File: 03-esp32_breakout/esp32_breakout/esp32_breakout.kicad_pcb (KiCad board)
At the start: 4 copper layers, 35 x 22.8 mm, 44 parts, among them J1 USB4110-GF-A, J2 Conn_01x06, SW1 SW_Push, SW2 SW_Push, SW3 SW_Push, U1 ESP32-S3, U3 AP2112H, Y1 ECS-400-10-37B2-CKY-TR, Y2 ECS-.327-12.5-34B-TR

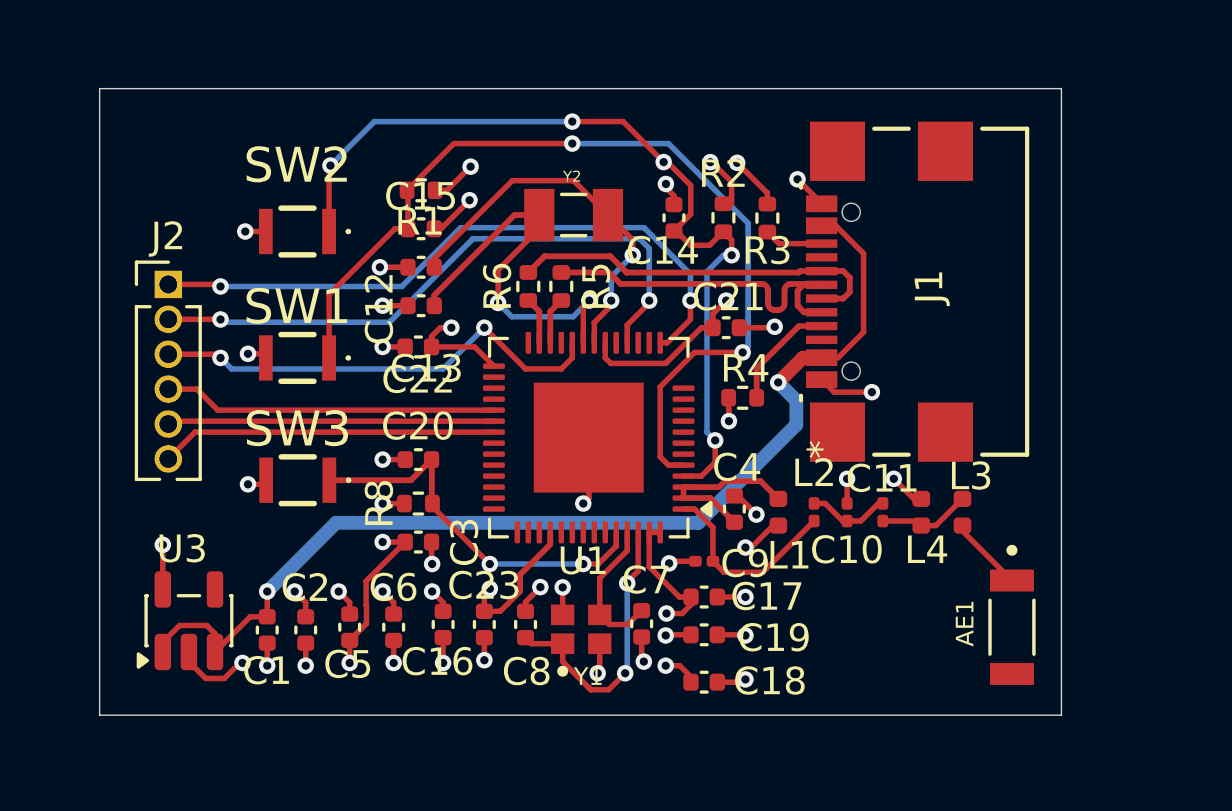
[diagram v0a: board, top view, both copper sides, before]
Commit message: layout improvement
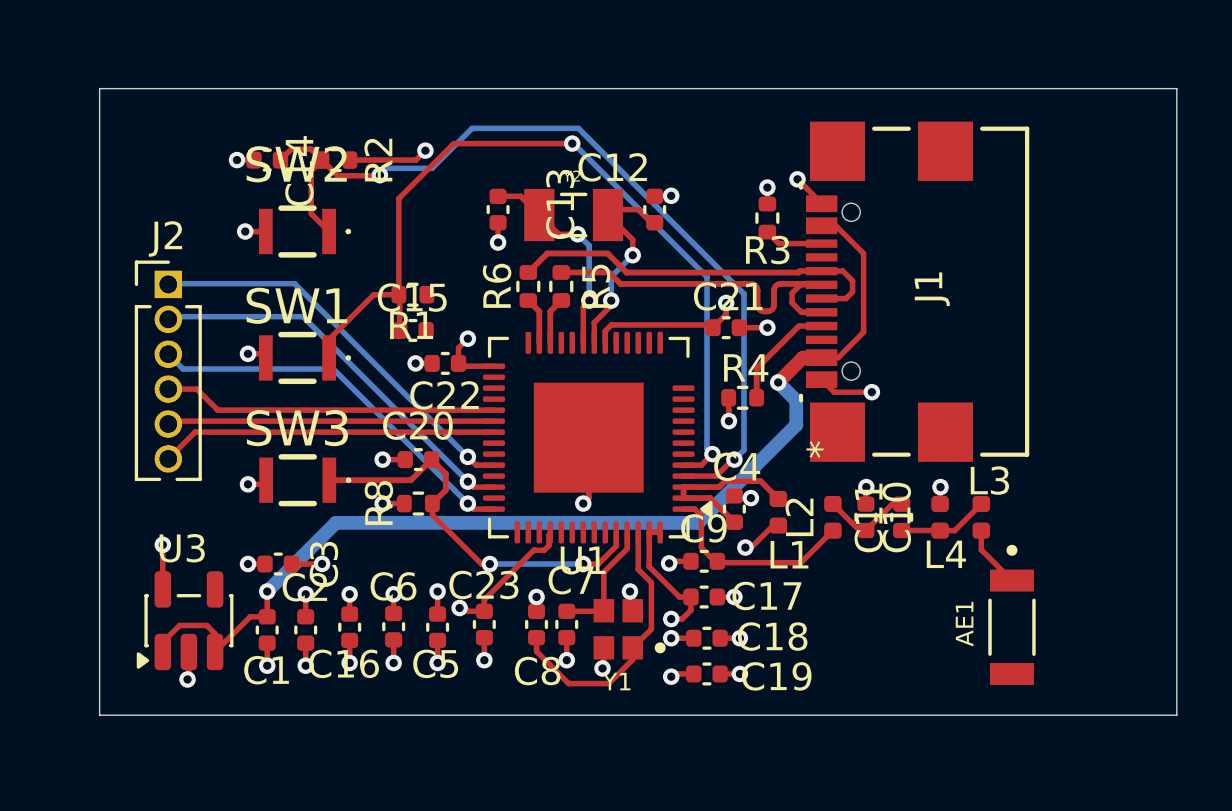
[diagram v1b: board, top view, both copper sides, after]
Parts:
- C10, C11, C9: footprint Capacitor_SMD:C_0201_0603Metric -> Capacitor_SMD:C_0402_1005Metric
- L2: footprint Inductor_SMD:L_0201_0603Metric -> Inductor_SMD:L_0402_1005Metric
- moved C14 14.9 mm to (153.5, 50.6), turned to 180 degrees
- moved R2 14.3 mm to (156.0, 50.6), turned to 0 degrees
- moved C12 8.76 mm to (167.6, 52.4), turned to -90 degrees
- moved C3 5.16 mm to (153.9, 65.3)
- moved C13 4.48 mm to (161.9, 52.4), turned to 90 degrees
- moved R1 3.81 mm to (158.8, 55.5)
- moved C15 3.71 mm to (158.8, 56.8)
- moved C16 3.40 mm to (156.5, 67.6)
- moved C5 3.20 mm to (159.7, 67.6)
- moved C7 2.73 mm to (164.4, 67.5)
- moved C18 1.60 mm to (169.5, 68.0)
- moved C19 1.43 mm to (169.5, 69.3)
- moved Y1 1.35 mm to (166.3, 67.7), turned to 90 degrees
- moved C22 1.15 mm to (160.0, 58.0)
- moved C10 0.71 mm to (175.3, 63.6)
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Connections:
- U1 pad 15: CS_FLASH -> unconnected-(U1-GPIO10-Pad15)
- U1 pad 18: CS_DAC -> unconnected-(U1-GPIO13-Pad18)
- U1 pad 23: CS_ADC -> unconnected-(U1-GPIO17-Pad23)
- U1 pad 38: unconnected-(U1-GPIO33-Pad38) -> CS_FLASH
- U1 pad 40: unconnected-(U1-GPIO35-Pad40) -> CS_DAC
- U1 pad 42: unconnected-(U1-GPIO37-Pad42) -> CS_ADC
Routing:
- net GND: track 42.8 -> 28.2 mm, vias 34 -> 33
- net CS_FLASH: track 23.7 -> 14.6 mm, vias 2 -> 1
- net CS_DAC: track 22.8 -> 14.5 mm, vias 2 -> 1
- net Net-(U1-XTAL_32K_N): track 15.2 -> 8.35 mm
- net Net-(U1-XTAL_32K_P): track 13.9 -> 7.58 mm
- net  VDD3P3_RTC: track 34.6 -> 31.0 mm, vias 16 -> 15
- net GPIO0: track 33.7 -> 30.5 mm
- net CS_ADC: track 16.9 -> 14.2 mm, vias 2 -> 1
- net Net-(U1-XTAL_N): track 5.29 -> 4.56 mm
- net Net-(C10-Pad2): track 3.03 -> 3.62 mm
- net GPIO46: track 14.1 -> 14.7 mm
- net Net-(U1-XTAL_P): track 10.4 -> 9.95 mm, vias 2 -> 0
- net Chip_PU: track 31.9 -> 32.2 mm, vias 5 -> 2
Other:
- board size 35 x 22.8 mm -> 39.2 x 22.8 mm

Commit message: ground zone
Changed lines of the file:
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@@
+	)
+	(segment
+		(start 168.18 51.92)
+		(end 167.6 51.92)
+		(width 0.2)
+		(layer "F.Cu")
+		(net 1)
 	)
 	(segment
@@
 	)
 	(segment
-		(start 168.18 51.92)
-		(end 168.2 51.9)
-		(width 0.2)
-		(layer "F.Cu")
-		(net 1)
-	)
-	(segment
 		(start 177.985 63.115)
 		(end 177.985 62.515)
@@
 	)
 	(segment
+		(start 168.3 51.8)
+		(end 168.18 51.92)
+		(width 0.2)
+		(layer "F.Cu")
+		(net 1)
+	)
+	(segment
 		(start 177.985 62.515)
 		(end 178 62.5)
@@
 	)
 	(segment
-		(start 167.6 51.92)
-		(end 168.18 51.92)
-		(width 0.2)
-		(layer "F.Cu")
-		(net 1)
-	)
-	(segment
 		(start 170.29 59.69)
 		(end 170.29 59.25)
@@
 	)
 	(via
-		(at 168.2 51.9)
+		(at 168.3 51.8)
 		(size 0.6)
 		(drill 0.3)
@@
 		(polygon
 			(pts
-				(xy 156.6 22.6) (xy 157 36) (xy 178.8 35.9) (xy 177.1 21.7)
-			)
-		)
-	)
-	(zone
-		(net 0)
-		(net_name "")
-		(layer "In1.Cu")
-		(hatch edge 0.5)
-		(connect_pads
-			(clearance 0)
-		)
-		(min_thickness 0.25)
-		(filled_areas_thickness no)
-		(keepout
-			(tracks allowed)
-			(vias allowed)
-			(pads allowed)
-			(copperpour not_allowed)
-			(footprints allowed)
-		)
-		(placement
-			(enabled no)
-			(sheetname "/")
-		)
-		(fill
-			(thermal_gap 0.5)
-			(thermal_bridge_width 0.5)
-		)
-		(polygon
-			(pts
-				(xy 160.9 50.8) (xy 168.9 50.8) (xy 168.9 57.9) (xy 160.9 57.8)
+				(xy 161.3 51.3) (xy 168.6 51.3) (xy 168.6 57.6) (xy 161.3 57.5)
 			)
 		)
@@
 		(polygon
 			(pts
-				(xy 140.75 44) (xy 192 43.5) (xy 192 78) (xy 139.25 77)
+				(xy 192 78) (xy 139.25 77) (xy 140.75 44) (xy 192 43.5)
 			)
 		)
+		(polygon
+			(pts
+				(xy 162.5 63.6) (xy 162.5 70) (xy 167.5 69.9) (xy 167.5 63.5)
+			)
+		)
+		(polygon
+			(pts
+				(xy 160.9 57.9) (xy 168.9 57.9) (xy 168.9 50.7) (xy 160.9 50.7)
+			)
+		)
+	)
+	(zone
+		(net 1)
+		(net_name "GND")
+		(layer "In1.Cu")
+		(hatch edge 0.5)
+		(priority 3)
+		(connect_pads yes
+			(clearance 0)
+		)
+		(min_thickness 0.25)
+		(filled_areas_thickness no)
+		(fill yes
+			(thermal_gap 0.5)
+			(thermal_bridge_width 0.5)
+		)
+		(polygon
+			(pts
+				(xy 167.3 63.8) (xy 167.3 69.5) (xy 162.8 69.5) (xy 162.8 63.8)
+			)
+		)

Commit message: updated atenna layout
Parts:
- moved C3 3.88 mm to (150.1, 64.5)
- moved C8 3.53 mm to (166.8, 67.7)
- moved C9 3.45 mm to (172.3, 63.4), turned to -90 degrees
- moved C2 3.37 mm to (153.2, 64.8), turned to 180 degrees
- moved L4 2.40 mm to (180.4, 63.6)
- moved L3 2.27 mm to (181.6, 64.5)
- moved C11 2.21 mm to (178.8, 63.9), turned to 180 degrees
- moved Y1 1.24 mm to (165.0, 67.7)
- moved C7 1.19 mm to (163.2, 67.6)
- moved C10 1.01 mm to (175.6, 64.5), turned to 90 degrees
- moved L1 0.86 mm to (171.3, 63.1)
- moved AE1 0.59 mm to (180.7, 68.2)
- moved C4 0.54 mm to (170.0, 63.1), turned to 90 degrees
- moved L2 0.38 mm to (173.9, 63.9), turned to 0 degrees
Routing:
- net  VDD3P3_RTC: track 31.0 -> 48.5 mm, vias 15 -> 11
- net Net-(U1-XTAL_P): track 9.95 -> 6.12 mm
- net Net-(C4-Pad2): track 6.42 -> 3.10 mm
- net Net-(C11-Pad1): track 3.54 -> 2.37 mm
- net Net-(C10-Pad2): track 3.62 -> 4.62 mm, vias 0 -> 1
- net Net-(U1-LNA_IN): track 7.41 -> 6.83 mm
- net Net-(U1-XTAL_N): track 4.56 -> 5.07 mm

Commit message: l
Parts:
- moved R6 8.76 mm to (171.8, 55.2), turned to 180 degrees
- moved R4 8.67 mm to (171.9, 50.6)
- moved R5 7.70 mm to (171.8, 56.5), turned to 180 degrees
- moved C21 2.72 mm to (167.6, 55.9)
- moved C4 1.99 mm to (170.7, 61.3), turned to -90 degrees
- moved L1 1.94 mm to (171.9, 61.3)
- moved AE1 1.56 mm to (181.0, 69.7)
- moved J1 1.12 mm to (178.2, 55.4)
- moved R3 1.12 mm to (172.8, 52.8)
- moved C11 0.97 mm to (178.5, 64.8)
- moved L3 0.75 mm to (181.6, 65.3)
- moved L4 0.74 mm to (180.2, 64.3)
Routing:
- net USB_D-: track 14.1 -> 3.24 mm
- net USB_D+: track 14.2 -> 3.91 mm
- net Net-(J1-CC1): track 4.07 -> 12.1 mm, vias 0 -> 2
- net /ESP_USB_D+: track 1.71 -> 8.82 mm
- net Chip_PU: track 32.2 -> 25.4 mm
- net /ESP_USB_D-: track 1.71 -> 7.31 mm
- net Net-(U1-LNA_IN): track 6.83 -> 5.01 mm
- net GND: track 28.4 -> 27.0 mm, vias 33 -> 65
- net Net-(C4-Pad2): track 3.10 -> 4.26 mm
- net Net-(C10-Pad2): track 4.62 -> 3.86 mm, vias 1 -> 0
- net  VDD3P3_RTC: track 48.5 -> 47.8 mm
- net Net-(AE1-FEED): track 1.83 -> 2.46 mm
- added copper zone on F.Cu, net GND
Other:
- board size 39.2 x 22.8 mm -> 35 x 24 mm

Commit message: finish layout
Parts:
- moved R5 2.33 mm to (170.4, 58.4)
- moved R6 2.19 mm to (170.4, 57.0)
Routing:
- net USB_D-: track 3.24 -> 8.08 mm
- net USB_D+: track 3.91 -> 7.59 mm
- net /ESP_USB_D-: track 7.31 -> 8.18 mm

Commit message: fixed a few things
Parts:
- added J4: GRPB021VWVN-RC, Connector_PinHeader_1.27mm:PinHeader_1x02_P1.27mm_Vertical, F.Cu at (160.7, 70.7)
- AE1: value Antenna_Chip -> XDCR_2459AT18B100E
- C7, C8: value 14µF -> 14pF
- J2: value Conn_01x06 -> GRPB061VWVN-RC
- U3: value AP2112H -> AP2112K
- moved C7 0.29 mm to (163.5, 67.6)
- moved C8 0.29 mm to (167.1, 67.7)
- moved Y1 0.29 mm to (165.3, 67.7)
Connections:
- U1 pad 49: unconnected-(U1-U0TXD-Pad49) -> TX
- U1 pad 50: unconnected-(U1-U0RXD-Pad50) -> RX
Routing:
- net TX: track 0.00 -> 11.4 mm
- net RX: track 0.00 -> 8.78 mm

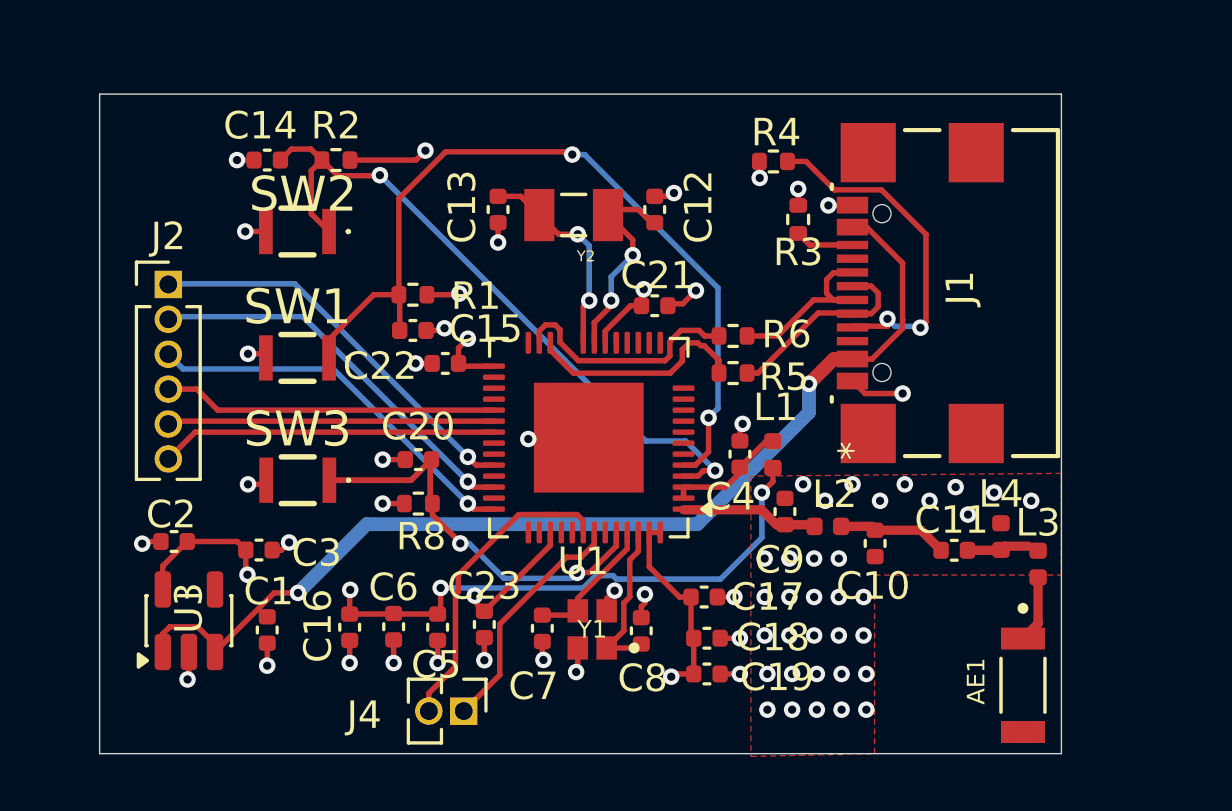
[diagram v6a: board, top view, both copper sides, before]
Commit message: added more breakout pins + added back silkscreen
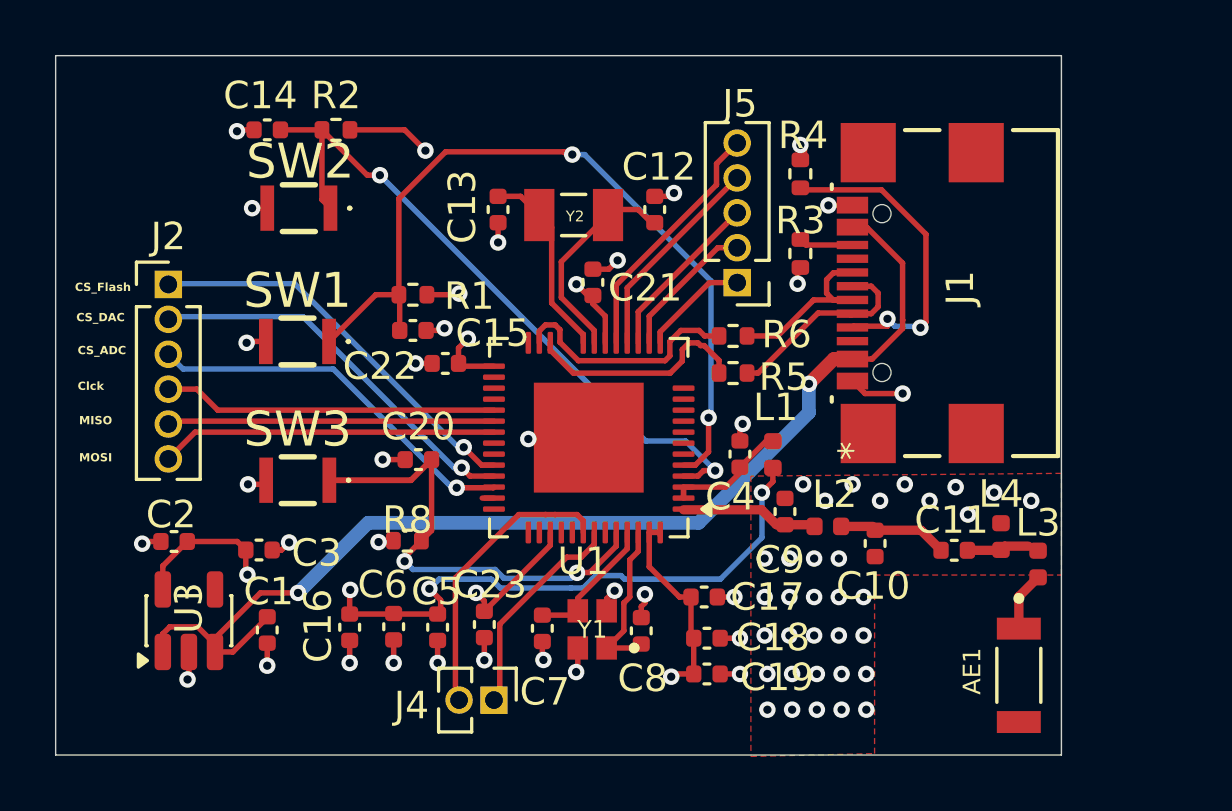
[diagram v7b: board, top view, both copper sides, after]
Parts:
- added G***: BJR_LOGO, wsg_fp:BJR_LOGO, B.Cu at (161.7, 51.0)
- added J5: GRPB051VWVN-RC, Connector_PinHeader_1.27mm:PinHeader_1x05_P1.27mm_Vertical, F.Cu at (170.6, 55.1)
- moved C21 2.41 mm to (165.3, 55.0), turned to -90 degrees
- moved R8 1.41 mm to (158.6, 64.5)
- moved R3 1.24 mm to (172.9, 54.0), turned to -90 degrees
- moved J4 1.17 mm to (161.8, 70.2)
- moved C14 1.10 mm to (153.5, 49.5)
- moved R2 1.10 mm to (156.0, 49.5)
- moved R4 1.08 mm to (172.9, 51.1), turned to 90 degrees
- moved SW2 0.85 mm to (154.7, 52.4)
- moved SW1 0.60 mm to (154.6, 57.2)
- moved AE1 0.39 mm to (180.8, 69.3)
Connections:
- U1 pad 15: unconnected-(U1-GPIO10-Pad15) -> GPIO10
- U1 pad 16: unconnected-(U1-GPIO11-Pad16) -> GPIO11
- U1 pad 17: unconnected-(U1-GPIO12-Pad17) -> GPIO12
- U1 pad 18: unconnected-(U1-GPIO13-Pad18) -> GPIO13
- U1 pad 19: unconnected-(U1-GPIO14-Pad19) -> GPIO14
- U1 pad 39: unconnected-(U1-GPIO34-Pad39) -> CS_DAC
- U1 pad 40: CS_DAC -> CS_ADC
- U1 pad 41: unconnected-(U1-GPIO36-Pad41) -> GPIO36
- U1 pad 42: CS_ADC -> GPIO37
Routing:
- net GPIO14: track 0.00 -> 9.09 mm
- net GPIO13: track 0.00 -> 7.66 mm
- net GPIO12: track 0.00 -> 6.22 mm
- net GPIO11: track 0.00 -> 5.20 mm
- net GPIO10: track 0.00 -> 3.94 mm
- net 5v_USB_EXT: track 38.7 -> 41.5 mm
- net GPIO46: track 14.8 -> 17.2 mm
- net Net-(J1-CC1): track 12.5 -> 11.6 mm
- net RX: track 8.78 -> 7.92 mm
- net  VDD3P3_RTC: track 47.9 -> 48.7 mm
- net Net-(U1-XTAL_32K_N): track 8.35 -> 7.59 mm, vias 2 -> 0
- net TX: track 11.4 -> 10.6 mm
- net Net-(U1-XTAL_32K_P): track 7.58 -> 7.83 mm, vias 2 -> 0
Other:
- board size 35 x 24 mm -> 36.6 x 25.5 mm
- board text added: "BJR @ JHU 22XT Esp32 Breakout"
- board text added: "CS_ADC"
- board text added: "CS_DAC"
- board text added: "CS_Flash"
- board text added: "Clck"
- board text added: "Emma Ouyang"
- board text added: "MISO"
- board text added: "MOSI"
- board text added: "Max Gao"
- board text added: "Sophie Noureddine"

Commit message: fixed decoupling cap layout
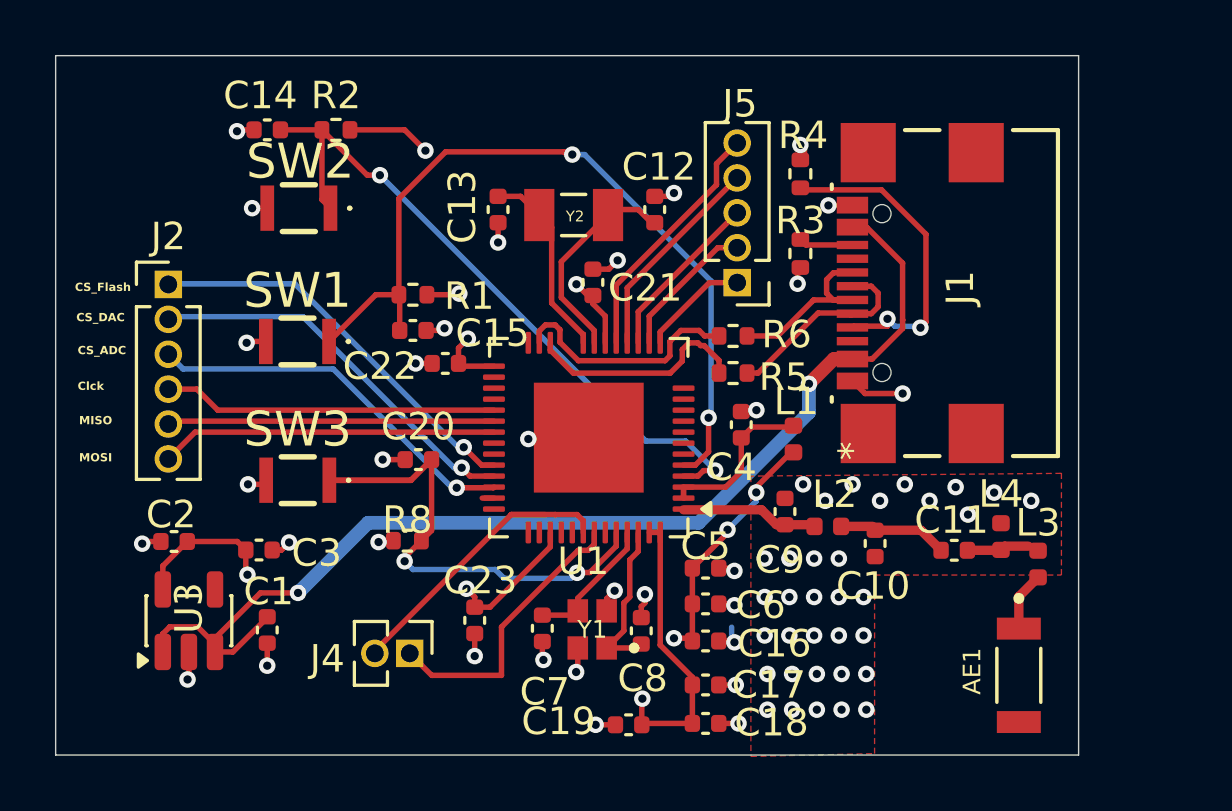
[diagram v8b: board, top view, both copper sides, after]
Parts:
- moved C16 13.0 mm to (169.4, 68.1), turned to 180 degrees
- moved C6 11.4 mm to (169.4, 66.8), turned to 180 degrees
- moved C5 9.98 mm to (169.4, 65.5), turned to 180 degrees
- moved J4 3.50 mm to (158.7, 68.5)
- moved C19 3.40 mm to (166.7, 71.2), turned to 0 degrees
- moved C17 3.20 mm to (169.4, 69.7)
- moved C18 3.10 mm to (169.4, 71.1)
- moved C4 1.07 mm to (170.8, 60.2)
- moved L1 0.94 mm to (172.7, 60.8)
- moved C23 0.38 mm to (161.1, 67.3)
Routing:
- net  VDD3P3_RTC: track 48.7 -> 40.2 mm
- net RX: track 7.92 -> 10.5 mm
- net Net-(C4-Pad2): track 4.26 -> 6.04 mm
- net TX: track 10.6 -> 11.7 mm
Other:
- board size 36.6 x 25.5 mm -> 37.2 x 25.5 mm
